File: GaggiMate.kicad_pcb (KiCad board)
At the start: 2 copper layers, 46 x 90 mm, 27 parts, among them K3 Relay, K4 Relay, Q1 2N7002, Q2 2N7002, Q3 2N7002, Q4 2N7002, U1 ESP32-S3-WROOM-1, U2 MAX31855KASA, U3 ADS1115IDGS, U4 ESP LDO, U5 LILY LDO

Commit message: attempt a HV stepdown and some PCB stuff
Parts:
- removed U5: LILY LDO, Package_DFN_QFN:DFN-6-1EP_3x3mm_P0.95mm_EP1.7x2.6mm
- added D3: 1N4007, Diode_THT:D_DO-41_SOD81_P10.16mm_Horizontal, F.Cu at (81.9, 92.4)
- added D4: 1N4007, Diode_THT:D_DO-41_SOD81_P10.16mm_Horizontal, F.Cu at (81.9, 96.7)
- added D5: 1N4007, Diode_THT:D_DO-41_SOD81_P10.16mm_Horizontal, F.Cu at (81.9, 100.9)
- added D6: 1N4007, Diode_THT:D_DO-41_SOD81_P10.16mm_Horizontal, F.Cu at (81.9, 105.2)
- added J13: ESP out, Connector_PinHeader_2.54mm:PinHeader_1x24_P2.54mm_Vertical, F.Cu at (120.5, 116.0)
- U4: value ESP LDO -> AMS1117-3.3; footprint Package_DFN_QFN:DFN-6-1EP_3x3mm_P0.95mm_EP1.7x2.6mm -> Package_TO_SOT_SMD:SOT-223-3_TabPin2
- moved U2 28.5 mm to (89.0, 60.9)
- moved U4 17.3 mm to (100.8, 94.5)
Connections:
- K3 pad 13: /Pump Relay/IN -> HV_L
- K4 pad 13: /Valve Relay/IN -> HV_L
- U1 pad 24: ALT? -> ALT
- U4 pad 2: 5V -> 3.3V

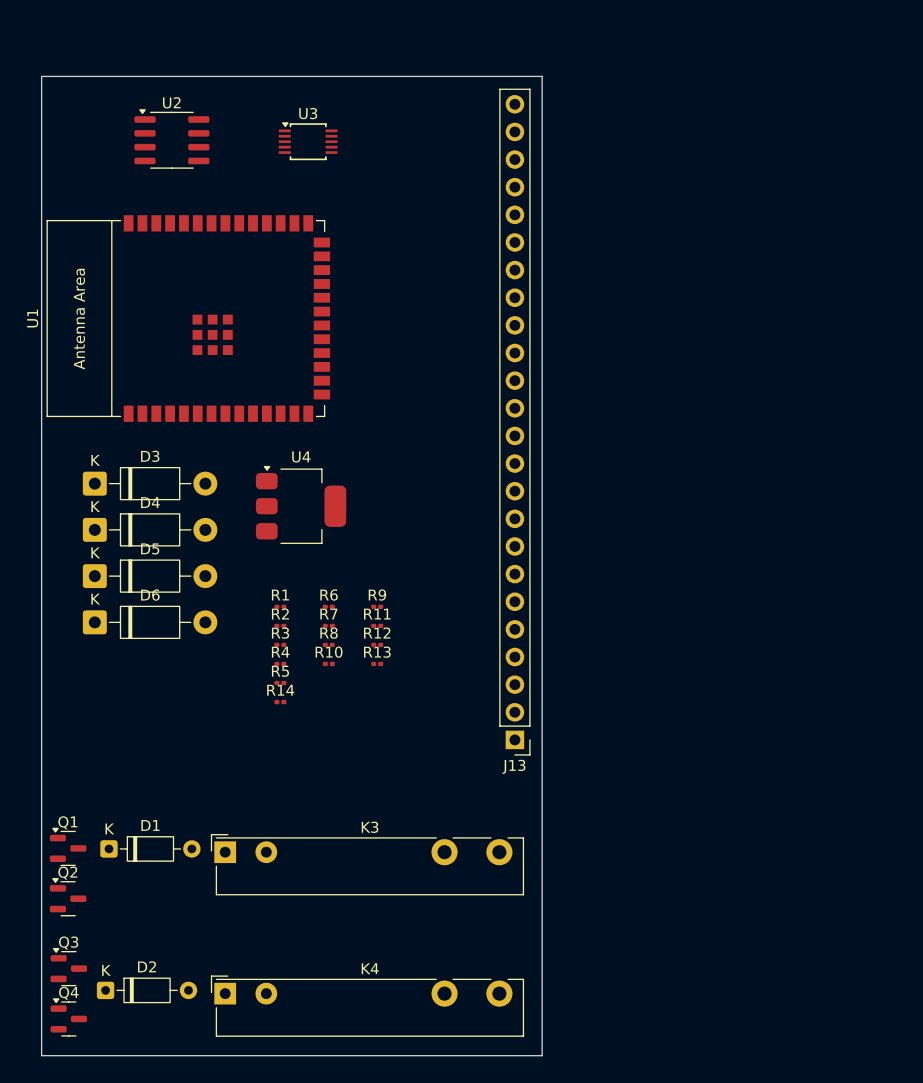
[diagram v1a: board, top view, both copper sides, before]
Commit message: update footprints, add 230v module, use SSRs and do some basic layouting
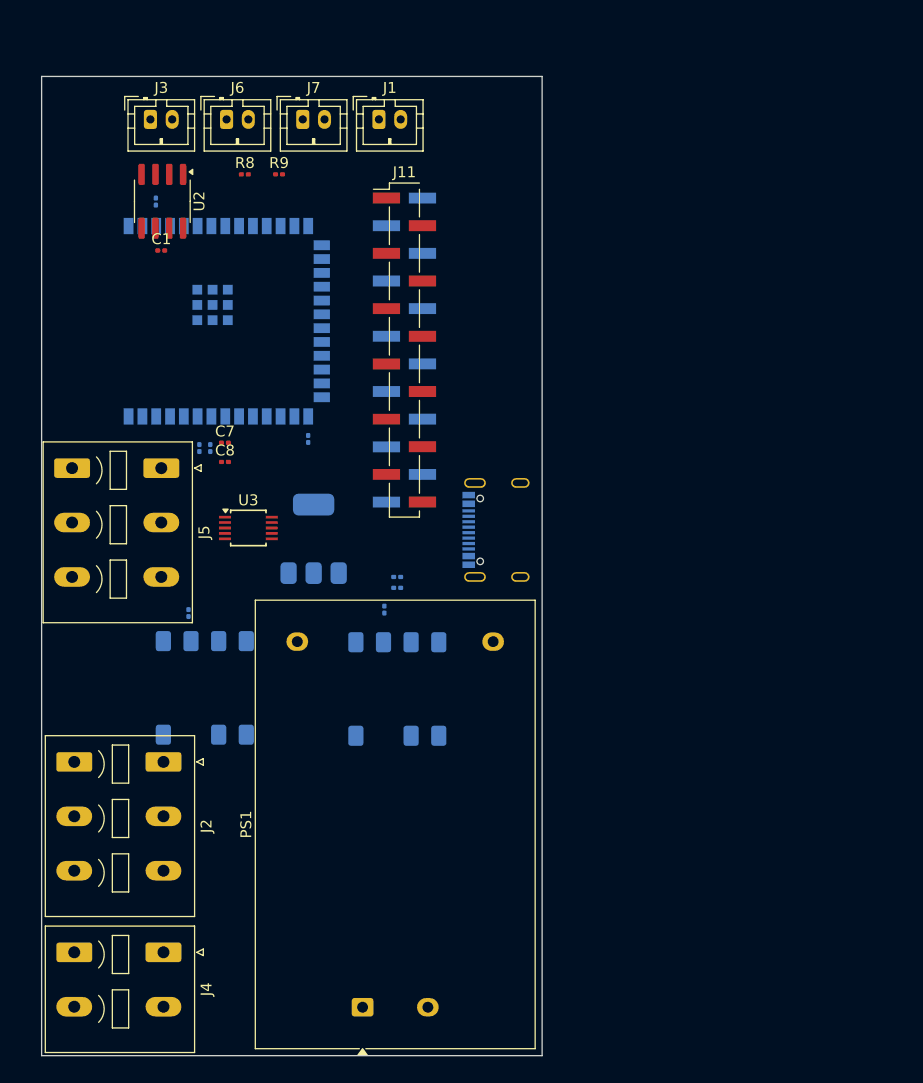
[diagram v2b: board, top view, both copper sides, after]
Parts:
- removed D1, D2: 1N4148, Diode_THT:D_DO-35_SOD27_P7.62mm_Horizontal
- removed D3, D4, D5, D6: 1N4007, Diode_THT:D_DO-41_SOD81_P10.16mm_Horizontal
- removed J13: ESP out, Connector_PinHeader_2.54mm:PinHeader_1x24_P2.54mm_Vertical
- removed K3, K4: Relay, Relay_THT:Relay_SPST-NO_Fujitsu_FTR-LYAA005x_FormA_Vertical
- removed Q1, Q2, Q3, Q4: 2N7002, Package_TO_SOT_SMD:SOT-23
- removed R1, R2: 10k, Resistor_SMD:R_0201_0603Metric
- removed R10, R11: 100k, Resistor_SMD:R_0201_0603Metric
- removed R12, R13: 4.7k, Resistor_SMD:R_0201_0603Metric
- added C1: 0.1µ, Capacitor_SMD:C_0201_0603Metric, F.Cu at (88.0, 71.0)
- added C2: 22µ, Capacitor_SMD:C_0201_0603Metric, B.Cu at (109.7, 101.0)
- added C3: 10µ, Capacitor_SMD:C_0201_0603Metric, B.Cu at (109.7, 102.0)
- added C7: 0.1µ, Capacitor_SMD:C_0201_0603Metric, F.Cu at (93.8, 88.7)
- added C8: 0.1µ, Capacitor_SMD:C_0201_0603Metric, F.Cu at (93.8, 90.4)
- added J1: Heater SSR, Connector_JST:JST_PH_B2B-PH-K_1x02_P2.00mm_Vertical, F.Cu at (108.0, 59.0)
- added J11: Conn_01x12_Pin, Connector_PinHeader_2.54mm:PinHeader_1x12_P2.54mm_Vertical_SMD_Pin1Left, F.Cu at (110.3, 80.2)
- added J2: JL142R-50803GA1, Connector_Phoenix_SPT:PhoenixContact_SPT_2.5_3-V-5.0-EX_1x03_P5.0mm_Vertical, F.Cu at (88.2, 118.0)
- added J3: K-Type probe, Connector_JST:JST_PH_B2B-PH-K_1x02_P2.00mm_Vertical, F.Cu at (87.0, 59.0)
- added J4: JL142R-50802GA1, Connector_Phoenix_SPT:PhoenixContact_SPT_2.5_2-V-5.0-EX_1x02_P5.0mm_Vertical, F.Cu at (88.2, 135.5)
- added J5: Pressure Sensor, Connector_Phoenix_SPT:PhoenixContact_SPT_2.5_3-V-5.0-EX_1x03_P5.0mm_Vertical, F.Cu at (88.0, 91.0)
- added J6: Brew BTN, Connector_JST:JST_PH_B2B-PH-K_1x02_P2.00mm_Vertical, F.Cu at (94.0, 59.0)
- added J7: Steam BTN, Connector_JST:JST_PH_B2B-PH-K_1x02_P2.00mm_Vertical, F.Cu at (101.0, 59.0)
- added J8: Conn_01x12_Pin, Connector_PinHeader_2.54mm:PinHeader_1x12_P2.54mm_Vertical_SMD_Pin1Left, B.Cu at (110.3, 80.2)
- added P1: USB_C_Plug_USB2.0, Connector_USB:USB_C_Receptacle_Palconn_UTC16-G, B.Cu at (118.8, 96.7)
- added PS1: HLK-5M05, Converter_ACDC:Converter_ACDC_Hi-Link_HLK-5Mxx, F.Cu at (106.5, 140.5)
- added U8: AQH2223A, Package_SO:SSO-7-8_6.4x9.78mm_P2.54mm, B.Cu at (92.0, 111.2)
- added U9: AQH2223A, Package_SO:SSO-7-8_6.4x9.78mm_P2.54mm, B.Cu at (109.7, 111.3)
- R14, R3, R4, R5, U1, U4: moved to B.Cu
- R6: value 4.7k -> 150; moved to B.Cu
- R7: value 100 -> 150; moved to B.Cu
- R8: value 4.7k -> 10k
- R9: value 100 -> 10k
- moved R8 43.9 mm to (95.7, 64.0)
- moved R3 42.3 mm to (87.5, 66.5), turned to -90 degrees
- moved R9 40.8 mm to (98.8, 64.0)
- moved U3 35.9 mm to (96.0, 96.5)
- moved R14 24.3 mm to (101.5, 88.3), turned to -90 degrees
- moved R5 22.5 mm to (92.5, 89.2), turned to 90 degrees
- moved R4 21.2 mm to (91.5, 89.2), turned to 90 degrees
- moved R6 12.9 mm to (90.5, 104.3), turned to -90 degrees
- moved U2 5.68 mm to (88.1, 66.5), turned to -90 degrees
- moved R7 5.32 mm to (108.5, 104.0), turned to -90 degrees
- moved U4 3.21 mm to (102.0, 97.5), turned to 90 degrees
- moved U1 0.25 mm to (93.2, 77.5), turned to -90 degrees
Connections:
- R6 pad 1: 5V -> VALVE
- R8 pad 1: 5V -> 3.3V
- R8 pad 2: Net-(D1-A) -> BREW_BTN
- R9 pad 1: VALVE -> STEAM_BTN
- R9 pad 2: Net-(Q3-G) -> 3.3V
- U2 pad 2: Net-(J3-Pin_2) -> /K-Probe T-
- U2 pad 3: Net-(J3-Pin_1) -> /K-Probe T+

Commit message: update some footprints etc
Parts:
- removed J11: Conn_01x12_Pin, Connector_PinHeader_2.54mm:PinHeader_1x12_P2.54mm_Vertical_SMD_Pin1Left
- removed J6: Brew BTN, Connector_JST:JST_PH_B2B-PH-K_1x02_P2.00mm_Vertical
- removed J7: Steam BTN, Connector_JST:JST_PH_B2B-PH-K_1x02_P2.00mm_Vertical
- added C4: C, Capacitor_SMD:C_0201_0603Metric, B.Cu at (112.5, 98.5)
- added D3: 1N5817, Diode_SMD:D_SOD-123, B.Cu at (112.5, 94.0)
- added J10: Analog sensors, easyeda2kicad:CONN-TH_3P-P2.54_DIBO_DB141V-2.54-3P, F.Cu at (82.5, 101.9)
- added J12: BTNS, Connector_JST:JST_PH_B4B-PH-K_1x04_P2.00mm_Vertical, F.Cu at (94.5, 59.0)
- added R1: 3.3k, Resistor_SMD:R_0201_0603Metric, B.Cu at (93.7, 86.0)
- added R10: 5.1k, Resistor_SMD:R_0201_0603Metric, B.Cu at (114.0, 98.5)
- added R11: 150, Resistor_SMD:R_0201_0603Metric, B.Cu at (100.4, 102.2)
- added R2: 5.1k, Resistor_SMD:R_0201_0603Metric, B.Cu at (114.0, 95.5)
- added R7: 68, Resistor_SMD:R_0201_0603Metric, B.Cu at (99.4, 102.2)
- added U5: USBLC6-2P6, Package_TO_SOT_SMD:SOT-666, B.Cu at (113.2, 97.0)
- C1, C7, C8, R8, R9, U2, U3: moved to B.Cu
- J2: value JL142R-50803GA1 -> Conn_01x02; footprint Connector_Phoenix_SPT:PhoenixContact_SPT_2.5_3-V-5.0-EX_1x03_P5.0mm_Vertical -> easyeda2kicad:CONN-TH_2P-P5.08_DIBO_DB142V-5.08-2P
- J3: footprint Connector_JST:JST_PH_B2B-PH-K_1x02_P2.00mm_Vertical -> easyeda2kicad:CONN-TH_2P-P2.54_DIBO_DB141V-2.54-2P
- J4: value JL142R-50802GA1 -> Conn_01x02; footprint Connector_Phoenix_SPT:PhoenixContact_SPT_2.5_2-V-5.0-EX_1x02_P5.0mm_Vertical -> easyeda2kicad:CONN-TH_2P-P5.08_DIBO_DB142V-5.08-2P
- J5: footprint Connector_Phoenix_SPT:PhoenixContact_SPT_2.5_3-V-5.0-EX_1x03_P5.0mm_Vertical -> easyeda2kicad:CONN-TH_3P-P2.54_DIBO_DB141V-2.54-3P
- moved C1 30.0 mm to (88.5, 101.0), turned to -90 degrees
- moved J1 21.0 mm to (87.0, 59.0)
- moved J3 20.6 mm to (107.5, 60.5), turned to 180 degrees
- moved U2 19.5 mm to (107.1, 71.0)
- moved C7 17.5 mm to (105.0, 102.2), turned to -90 degrees
- moved C8 15.2 mm to (103.5, 102.1), turned to 90 degrees
- moved J2 8.86 mm to (85.7, 126.5)
- moved U3 7.52 mm to (88.5, 97.0), turned to -90 degrees
- moved C3 7.18 mm to (102.5, 102.2), turned to -90 degrees
- moved J8 7.08 mm to (114.3, 74.3)
- moved J5 5.47 mm to (82.5, 91.4)
- moved R6 5.05 mm to (113.5, 104.7)
- moved J4 4.69 mm to (85.7, 139.5)
- moved R12 4.50 mm to (95.0, 104.5)
- moved C2 3.86 mm to (106.0, 102.2), turned to -90 degrees
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- renumbered R6 to R12, R7 to R6
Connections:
- J8 pad 11: VALVE -> /A10
- J8 pad 12: PUMP -> /A11
- J8 pad 6: SPI_MISO -> /A5
- J8 pad 7: SPI_MOSI -> /A6
- J8 pad 8: SPI_CLK -> /A7
- J8 pad 9: MAX_SPI_CS -> /A8
- P1 pad A4: 5V -> Net-(D3-A)
- P1 pad A5: NC -> Net-(P1-CC)
- P1 pad A6: USB_D+ -> Net-(P1-D+)
- P1 pad A7: USB_D- -> Net-(P1-D-)
- P1 pad A9: 5V -> Net-(D3-A)
- P1 pad B4: 5V -> Net-(D3-A)
- P1 pad B5: NC -> Net-(P1-VCONN)
- P1 pad B9: 5V -> Net-(D3-A)
- R12 pad 1: VALVE -> GND
- R12 pad 2: Net-(R6-Pad2) -> Net-(R12-Pad2)
- R6 pad 1: PUMP -> GND
- R6 pad 2: Net-(R7-Pad2) -> Net-(R6-Pad2)
- U1 pad 10: /A16 -> /A9
- U1 pad 11: /A17 -> /A10
- U1 pad 12: /A9 -> /A5
- U1 pad 16: /A21 -> /A13
- U1 pad 19: /A12 -> /A6
- U1 pad 20: /A13 -> /A7
- U1 pad 21: /A14 -> /A8
- U1 pad 23: /A18 -> /A11
- U1 pad 26: /A20 -> /A12
- U1 pad 28: NC -> unconnected-(U1-SPIIO6/GPIO35/FSPID/SUBSPID-Pad28)
- U1 pad 29: NC -> unconnected-(U1-SPIIO7/GPIO36/FSPICLK/SUBSPICLK-Pad29)
- U1 pad 30: NC -> unconnected-(U1-SPIDQS/GPIO37/FSPIQ/SUBSPIQ-Pad30)
- U1 pad 32: NC -> unconnected-(U1-MTCK/GPIO39/CLK_OUT3/SUBSPICS1-Pad32)
- U1 pad 8: NC -> unconnected-(U1-GPIO15/U0RTS/ADC2_CH4/XTAL_32K_P-Pad8)
- U1 pad 9: NC -> unconnected-(U1-GPIO16/U0CTS/ADC2_CH5/XTAL_32K_N-Pad9)
- U8 pad 1: GND -> Net-(R12-Pad2)
- U8 pad 2: Net-(R6-Pad2) -> VALVE
- U8 pad 3: GND -> Net-(R12-Pad2)
- U8 pad 4: GND -> Net-(R12-Pad2)
- U9 pad 1: GND -> Net-(R6-Pad2)
- U9 pad 2: Net-(R7-Pad2) -> PUMP
- U9 pad 3: GND -> Net-(R6-Pad2)
- U9 pad 4: GND -> Net-(R6-Pad2)

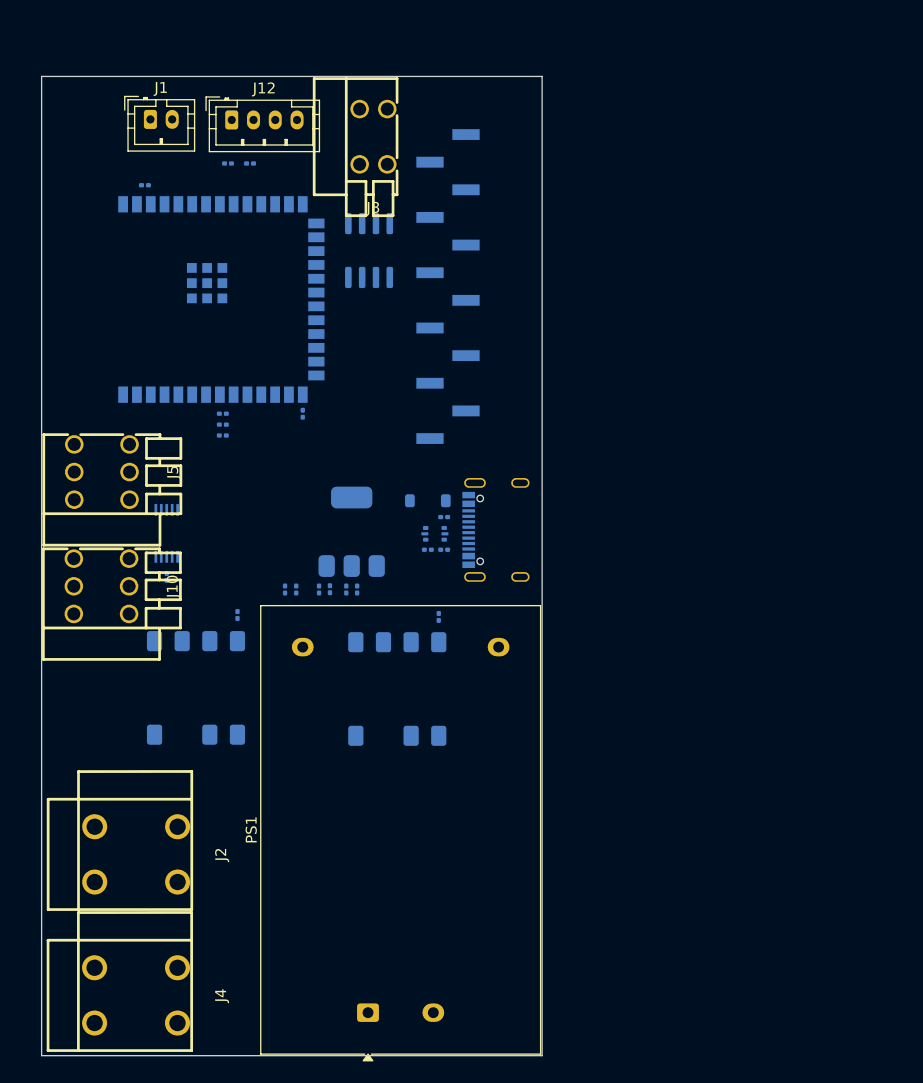
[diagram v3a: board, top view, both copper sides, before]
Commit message: Moved front side components to other board, finished cap and resistor selection and maybe finalizing layout
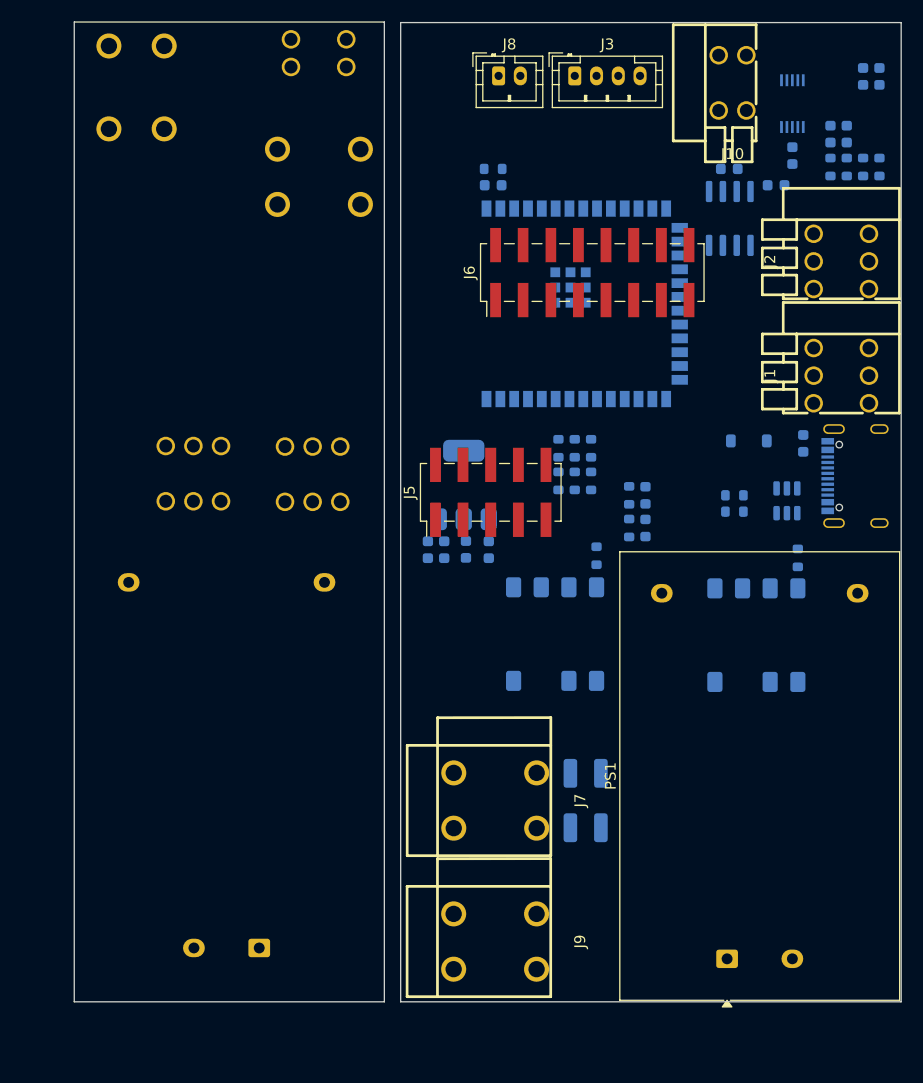
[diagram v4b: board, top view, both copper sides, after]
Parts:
- removed the J8 at (114.3, 74.3)
- removed the U5 at (113.2, 97.0)
- added C10: 0.1uF, Capacitor_SMD:C_0603_1608Metric, B.Cu at (144.5, 65.0)
- added C11: 10nF, Capacitor_SMD:C_0603_1608Metric, B.Cu at (140.2, 63.5)
- added C2: 22nF, Capacitor_SMD:C_0603_1608Metric, B.Cu at (151.0, 60.3)
- added C3: 10uF, Capacitor_SMD:C_0603_1608Metric, B.Cu at (147.0, 88.7)
- added C5: 22nF, Capacitor_SMD:C_0603_1608Metric, B.Cu at (152.5, 55.0)
- added C6: 22nF, Capacitor_SMD:C_0603_1608Metric, B.Cu at (154.0, 55.0)
- added C7: 10uF, Capacitor_SMD:C_0603_1608Metric, B.Cu at (118.5, 65.0)
- added D2: 5V LED, LED_SMD:LED_0603_1608Metric, B.Cu at (132.5, 96.5)
- added D3: 3.3V LED, LED_SMD:LED_0603_1608Metric, B.Cu at (132.5, 93.5)
- added J11: Pressure Sensor, easyeda2kicad:CONN-TH_3P-P2.54_DIBO_DB141V-2.54-3P, B.Cu at (91.0, 91.5)
- added J12: Analog sensors, easyeda2kicad:CONN-TH_3P-P2.54_DIBO_DB141V-2.54-3P, B.Cu at (101.9, 91.6)
- added J13: K-Type probe, easyeda2kicad:CONN-TH_2P-P2.54_DIBO_DB141V-2.54-2P, B.Cu at (102.5, 52.9)
- added J14: Relays, easyeda2kicad:CONN-TH_2P-P5.08_DIBO_DB142V-5.08-2P, B.Cu at (102.5, 64.2)
- added J15: HV In, easyeda2kicad:CONN-TH_2P-P5.08_DIBO_DB142V-5.08-2P, B.Cu at (85.7, 56.0)
- added J5: Debug Pins, Connector_PinHeader_2.54mm:PinHeader_2x05_P2.54mm_Vertical_SMD, F.Cu at (118.3, 93.2)
- added J6: Conn_02x08_Odd_Even, Connector_PinHeader_2.54mm:PinHeader_2x08_P2.54mm_Vertical_SMD, F.Cu at (127.6, 73.0)
- added PS2: HLK-5M05, Converter_ACDC:Converter_ACDC_Hi-Link_HLK-5Mxx, B.Cu at (97.0, 135.1)
- added R14: 845, Resistor_SMD:R_0603_1608Metric, B.Cu at (152.5, 63.3)
- added R15: 845, Resistor_SMD:R_0603_1608Metric, B.Cu at (154.0, 63.3)
- added R7: 845, Resistor_SMD:R_0603_1608Metric, B.Cu at (151.0, 63.3)
- added R9: 845, Resistor_SMD:R_0603_1608Metric, B.Cu at (149.5, 63.3)
- added RV1: Varistor, Diode_SMD:D_1210_3225Metric, B.Cu at (127.0, 119.0)
- added RV2: Varistor, Diode_SMD:D_1210_3225Metric, B.Cu at (127.0, 124.0)
- added U2: USBLC6-2SC6, Package_TO_SOT_SMD:SOT-23-6, B.Cu at (145.5, 94.0)
- C1, C8: value 0.1µ -> 0.1uF; footprint Capacitor_SMD:C_0201_0603Metric -> Capacitor_SMD:C_0603_1608Metric
- C12: renamed from C2; value 22µ -> 22uF; footprint Capacitor_SMD:C_0201_0603Metric -> Capacitor_SMD:C_0603_1608Metric
- C13: renamed from C7; value 0.1µ -> 0.1uF; footprint Capacitor_SMD:C_0201_0603Metric -> Capacitor_SMD:C_0603_1608Metric
- C4: value C -> 22nF; footprint Capacitor_SMD:C_0201_0603Metric -> Capacitor_SMD:C_0603_1608Metric
- C9: renamed from C3; value 10µ -> 10uF; footprint Capacitor_SMD:C_0201_0603Metric -> Capacitor_SMD:C_0603_1608Metric
- J7: renamed from J2; value Conn_01x02 -> Relays
- J9: renamed from J4; value Conn_01x02 -> HV In
- R1: renamed from R3; footprint Resistor_SMD:R_0201_0603Metric -> Resistor_SMD:R_0603_1608Metric
- R10: renamed from R11; value 150 -> 200; footprint Resistor_SMD:R_0201_0603Metric -> Resistor_SMD:R_0603_1608Metric
- R11: renamed from R5; footprint Resistor_SMD:R_0201_0603Metric -> Resistor_SMD:R_0603_1608Metric
- R12: renamed from R1; footprint Resistor_SMD:R_0201_0603Metric -> Resistor_SMD:R_0603_1608Metric
- R13: renamed from R7; value 68 -> 150; footprint Resistor_SMD:R_0201_0603Metric -> Resistor_SMD:R_0603_1608Metric
- R16: renamed from R12; footprint Resistor_SMD:R_0201_0603Metric -> Resistor_SMD:R_0603_1608Metric
- R17: renamed from R6; footprint Resistor_SMD:R_0201_0603Metric -> Resistor_SMD:R_0603_1608Metric
- R2: renamed from R14; footprint Resistor_SMD:R_0201_0603Metric -> Resistor_SMD:R_0603_1608Metric
- R3: renamed from R8; footprint Resistor_SMD:R_0201_0603Metric -> Resistor_SMD:R_0603_1608Metric
- R4: renamed from R9; footprint Resistor_SMD:R_0201_0603Metric -> Resistor_SMD:R_0603_1608Metric
- R5: renamed from R2; footprint Resistor_SMD:R_0201_0603Metric -> Resistor_SMD:R_0603_1608Metric
- R6: renamed from R10; footprint Resistor_SMD:R_0201_0603Metric -> Resistor_SMD:R_0603_1608Metric
- R8: renamed from R4; footprint Resistor_SMD:R_0201_0603Metric -> Resistor_SMD:R_0603_1608Metric
- moved J1 70.7 mm to (150.5, 82.5), turned to 90 degrees
- moved J2 70.7 mm to (150.5, 72.0), turned to 90 degrees
- moved U1 69.8 mm to (146.0, 57.5)
- moved C1 69.3 mm to (146.0, 62.3)
- moved C4 53.2 mm to (149.5, 60.3), turned to -90 degrees
- moved R3 44.3 mm to (127.5, 92.2), turned to -90 degrees
- moved R4 40.7 mm to (124.5, 92.2), turned to 90 degrees
- moved R16 33.4 mm to (128.0, 99.0)
- moved R17 33.4 mm to (146.5, 99.2)
- moved U3 33.4 mm to (126.2, 75.9)
- moved J9 33.4 mm to (118.7, 134.5)
- moved PS1 33.4 mm to (140.0, 136.1)
- moved J10 33.4 mm to (140.5, 55.6)
- moved J7 33.4 mm to (118.7, 121.5)
- moved U6 33.4 mm to (124.2, 106.2)
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- renumbered D3 to D1, J10 to J1, J3 to J10, J5 to J2, J12 to J3, J1 to J8, U3 to U1, U1 to U3, U2 to U4, U4 to U5, U8 to U6, U9 to U7
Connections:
- C4 pad 1: Net-(D3-A) -> GND
- C4 pad 2: Net-(C4-Pad2) -> Net-(U1-AIN2)
- D1 pad 2: Net-(D3-A) -> Net-(D1-A)
- J1 pad 1: AIN1 -> AIN3
- J1 pad 3: AIN3 -> AIN1
- P1 pad A4: Net-(D3-A) -> Net-(D1-A)
- P1 pad A9: Net-(D3-A) -> Net-(D1-A)
- P1 pad B4: Net-(D3-A) -> Net-(D1-A)
- P1 pad B9: Net-(D3-A) -> Net-(D1-A)
- R5 pad 2: Net-(C4-Pad2) -> GND
- R6 pad 2: Net-(C4-Pad2) -> GND
- U1 pad 4: PRESSURE -> Net-(U1-AIN0)
- U1 pad 5: AIN1 -> Net-(U1-AIN1)
- U1 pad 6: AIN2 -> Net-(U1-AIN2)
- U1 pad 7: AIN3 -> Net-(U1-AIN3)
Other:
- board size 46 x 90 mm -> 76 x 90.1 mm
- copper layers 2 -> 4
